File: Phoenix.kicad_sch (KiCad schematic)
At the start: 0 parts

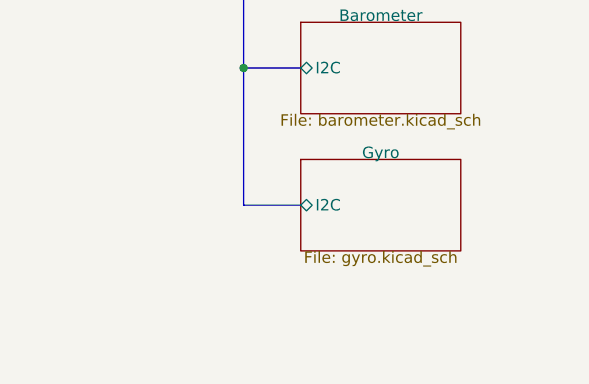
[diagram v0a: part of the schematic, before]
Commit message: Added pullup resistors
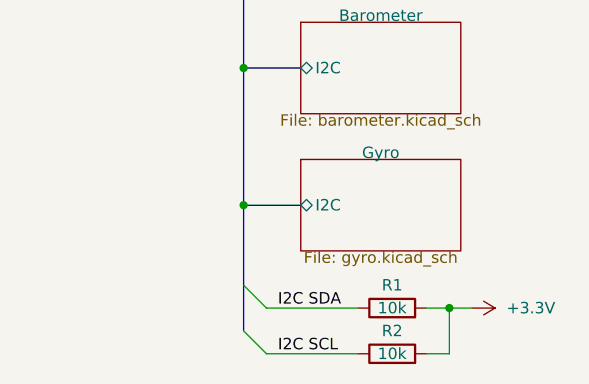
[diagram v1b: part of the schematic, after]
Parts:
- added R1, R2: 10k, symbol Device:R
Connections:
- new net +3V3: R1.2, R2.2
- new net I2C SCL: R2.1
- new net I2C SDA: R1.1
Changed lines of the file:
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@@
     (comment 1 "2022/10/18 WH")
   )
+  (junction (at 128.27 85.09) (diameter 0) (color 0 0 0 0)
+  )
   (junction (at 128.27 69.85) (diameter 0) (color 0 0 0 0)
   )
   (junction (at 128.27 54.61) (diameter 0) (color 0 0 0 0)
   )
+  (junction (at 151.13 96.52) (diameter 0) (color 0 0 0 0)
+  )
+  (bus_entry (at 130.81 96.52) (size -2.54 -2.54)
+    (stroke (width 0) (type default) (color 0 0 0 0))
+  )
+  (bus_entry (at 130.81 101.6) (size -2.54 -2.54)
+    (stroke (width 0) (type default) (color 0 0 0 0))
+  )
   (bus (pts (xy 128.27 46.99) (xy 128.27 36.83))
     (stroke (width 0) (type default) (color 0 0 0 0))
   )
+  (wire (pts (xy 151.13 101.6) (xy 148.59 101.6))
+    (stroke (width 0) (type default) (color 0 0 0 0))
+  )
+  (wire (pts (xy 148.59 96.52) (xy 151.13 96.52))
+    (stroke (width 0) (type default) (color 0 0 0 0))
+  )
   (bus (pts (xy 128.27 69.85) (xy 128.27 85.09))
     (stroke (width 0) (type default) (color 0 0 0 0))
@@
     (stroke (width 0) (type default) (color 0 0 0 0))
   )
+  (bus (pts (xy 128.27 93.98) (xy 128.27 99.06))
+    (stroke (width 0) (type default) (color 0 0 0 0))
+  )
+  (wire (pts (xy 151.13 96.52) (xy 153.67 96.52))
+    (stroke (width 0) (type default) (color 0 0 0 0))
+  )
+  (wire (pts (xy 130.81 101.6) (xy 140.97 101.6))
+    (stroke (width 0) (type default) (color 0 0 0 0))
+  )
   (bus (pts (xy 121.92 54.61) (xy 128.27 54.61))
     (stroke (width 0) (type default) (color 0 0 0 0))
@@
     (stroke (width 0) (type default) (color 0 0 0 0))
   )
+  (wire (pts (xy 130.81 96.52) (xy 140.97 96.52))
+    (stroke (width 0) (type default) (color 0 0 0 0))
+  )
   (bus (pts (xy 128.27 54.61) (xy 134.62 54.61))
     (stroke (width 0) (type default) (color 0 0 0 0))
   )
+  (bus (pts (xy 128.27 85.09) (xy 128.27 93.98))
+    (stroke (width 0) (type default) (color 0 0 0 0))
+  )
+  (wire (pts (xy 151.13 96.52) (xy 151.13 101.6))
+    (stroke (width 0) (type default) (color 0 0 0 0))
+  )
   (bus (pts (xy 128.27 85.09) (xy 134.62 85.09))
     (stroke (width 0) (type default) (color 0 0 0 0))
@@
   (bus (pts (xy 128.27 54.61) (xy 128.27 69.85))
     (stroke (width 0) (type default) (color 0 0 0 0))
+  )
+  (label "I2C SDA" (at 132.08 96.52 0)
+    (effects (font (size 1.27 1.27)) (justify left bottom))
+  )
+  (label "I2C SCL" (at 132.08 101.6 0)
+    (effects (font (size 1.27 1.27)) (justify left bottom))
+  )
+  (symbol (lib_id "Device:R") (at 144.78 101.6 90) (unit 1)
+    (in_bom yes) (on_board yes)
+    (property "Reference" "R2" (id 0) (at 144.78 99.06 90))
+    (property "Value" "10k" (id 1) (at 144.78 101.6 90))
+    (property "Footprint" "" (id 2) (at 144.78 103.378 90)
+      (effects (font (size 1.27 1.27)) hide)
+    )
+    (property "Datasheet" "~" (id 3) (at 144.78 101.6 0)
+      (effects (font (size 1.27 1.27)) hide)
+    )
+    (pin "1")
+    (pin "2")
+  )
+  (symbol (lib_id "Device:R") (at 144.78 96.52 90) (unit 1)
+    (in_bom yes) (on_board yes)
+    (property "Reference" "R1" (id 0) (at 144.78 93.98 90))
+    (property "Value" "10k" (id 1) (at 144.78 96.52 90))
+    (property "Footprint" "" (id 2) (at 144.78 98.298 90)
+      (effects (font (size 1.27 1.27)) hide)
+    )
+    (property "Datasheet" "~" (id 3) (at 144.78 96.52 0)
+      (effects (font (size 1.27 1.27)) hide)
+    )
+    (pin "1")
+    (pin "2")
+  )
+  (symbol (lib_id "power:+3.3V") (at 153.67 96.52 270) (unit 1)
+    (in_bom yes) (on_board yes) (fields_autoplaced)
+    (property "Reference" "#PWR?" (id 0) (at 149.86 96.52 0)
+      (effects (font (size 1.27 1.27)) hide)
+    )
+    (property "Value" "+3.3V" (id 1) (at 157.48 96.5199 90)
+      (effects (font (size 1.27 1.27)) (justify left))
+    )
+    (property "Footprint" "" (id 2) (at 153.67 96.52 0)
+      (effects (font (size 1.27 1.27)) hide)
+    )
+    (property "Datasheet" "" (id 3) (at 153.67 96.52 0)
+      (effects (font (size 1.27 1.27)) hide)
+    )
+    (pin "1")
   )
   (sheet (at 134.62 64.77) (size 17.78 10.16)
@@
       (reference "#PWR?") (unit 1) (value "GND") (footprint "")
     )
+    (path "/fdc5bc93-cd8d-4811-bebe-254f9b5ae1b6"
+      (reference "#PWR?") (unit 1) (value "+3.3V") (footprint "")
+    )
     (path "/973e92e2-e415-4dc5-9283-1d2d8aa34625/00b942de-1e62-476c-a78f-85d1dc0d5dee"
       (reference "C1") (unit 1) (value "100n") (footprint "Capacitor_SMD:C_0603_1608Metric")
@@
       (reference "R1") (unit 1) (value "27") (footprint "Resistor_SMD:R_0603_1608Metric_Pad0.98x0.95mm_HandSolder")
     )
+    (path "/db5533e2-fae3-4182-acad-2909cd70b23b"
+      (reference "R1") (unit 1) (value "10k") (footprint "")
+    )
     (path "/973e92e2-e415-4dc5-9283-1d2d8aa34625/365d1fd1-547e-42e3-ad75-f7c0cd8d8a12"
       (reference "R2") (unit 1) (value "27") (footprint "Resistor_SMD:R_0603_1608Metric_Pad0.98x0.95mm_HandSolder")
     )
+    (path "/c724a421-745b-4d41-9112-41d74b6d024a"
+      (reference "R2") (unit 1) (value "10k") (footprint "")
+    )
     (path "/973e92e2-e415-4dc5-9283-1d2d8aa34625/7239285e-3faf-4ba7-895f-832ed4958cbd"

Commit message: Experimented with git
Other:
- sheet Gyro renamed Accelerometer
- sheet Accelerometer: file gyro.kicad_sch -> accl.kicad_sch
- moved on the sheet: R1, R2

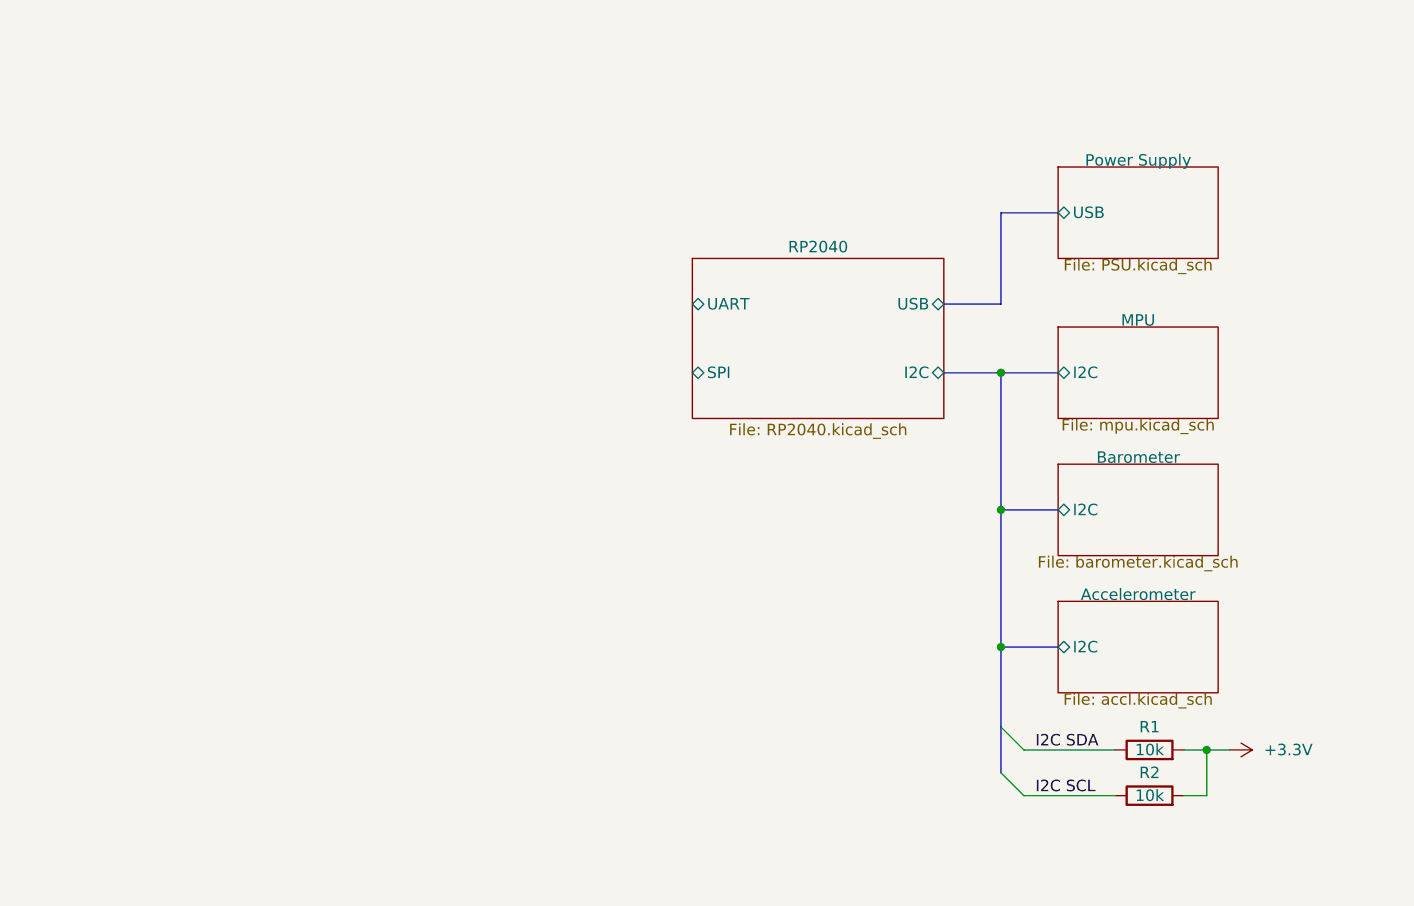
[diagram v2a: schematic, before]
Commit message: Added flash and radio submodules
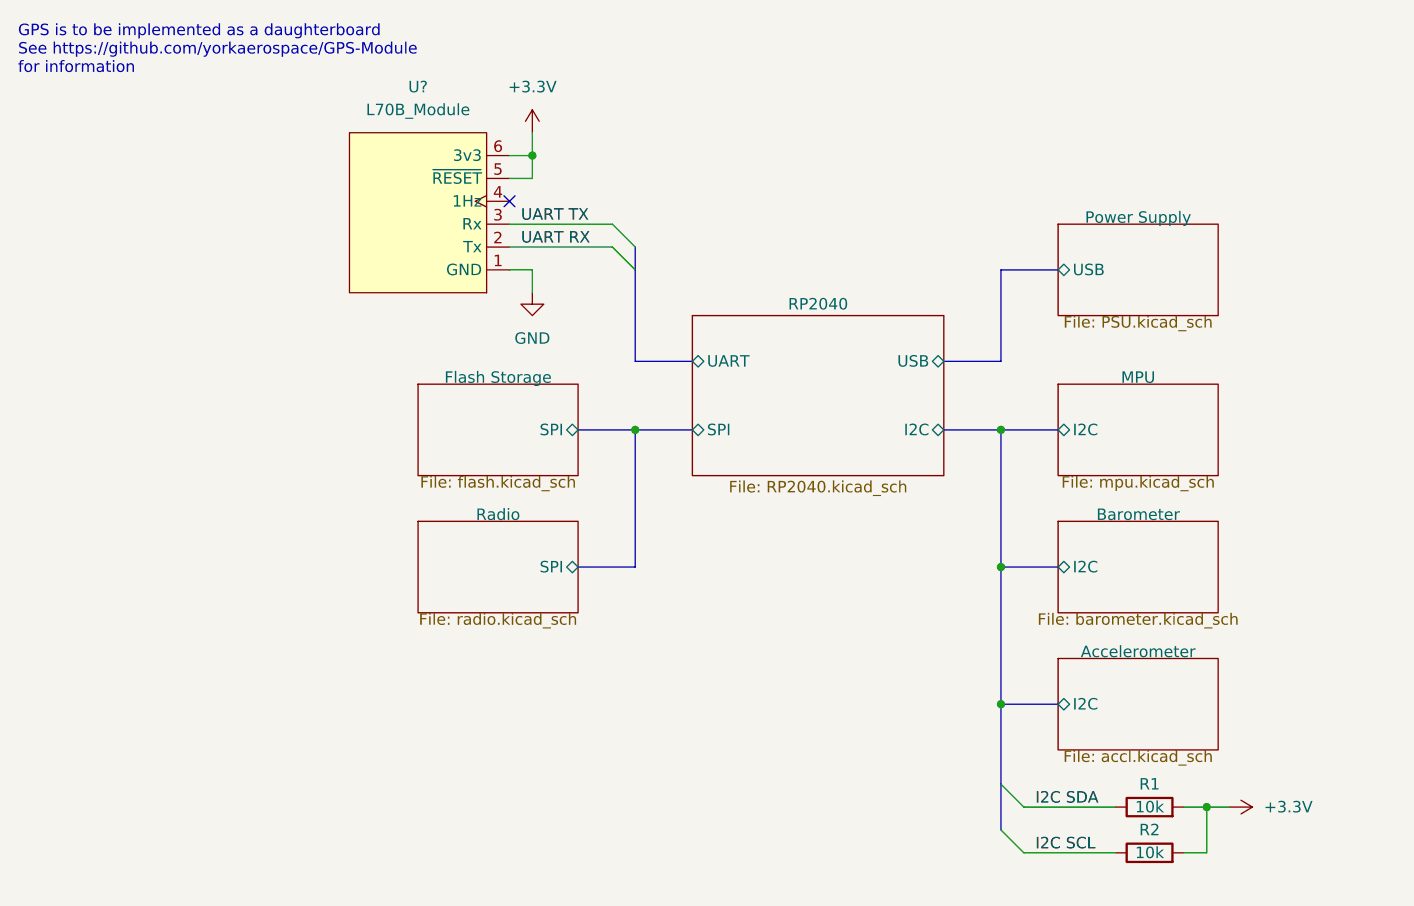
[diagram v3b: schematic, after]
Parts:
- added U?: L70B_Module, symbol GPS_Components:L70B_Module
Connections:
- net +3V3: now also U?.5 (~{RESET}), U?.6 (3v3)
- new net GND: U?.1 (GND)
- new net UART RX: U?.2 (Tx)
- new net UART TX: U?.3 (Rx)
- no-connect marks 0 -> 1
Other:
- added sheet Flash Storage (flash.kicad_sch)
- added sheet Radio (radio.kicad_sch)
- note added: "GPS is to be implemented as a daughterboard See https://github.com/yorkaerospace/GPS-Module for information"
- moved on the sheet: R1, R2

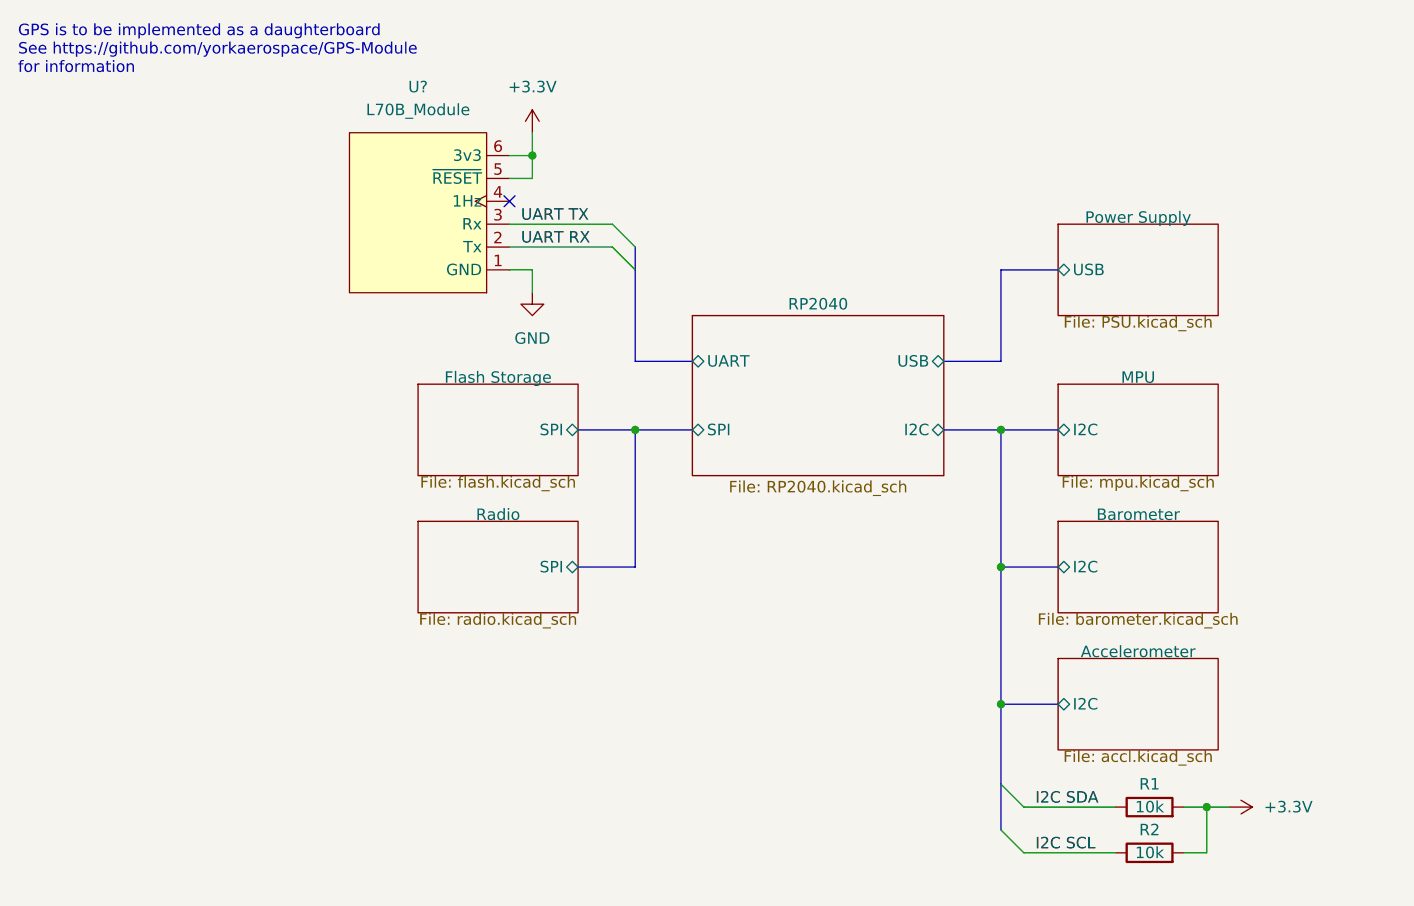
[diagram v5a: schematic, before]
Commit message: Fixed bus names
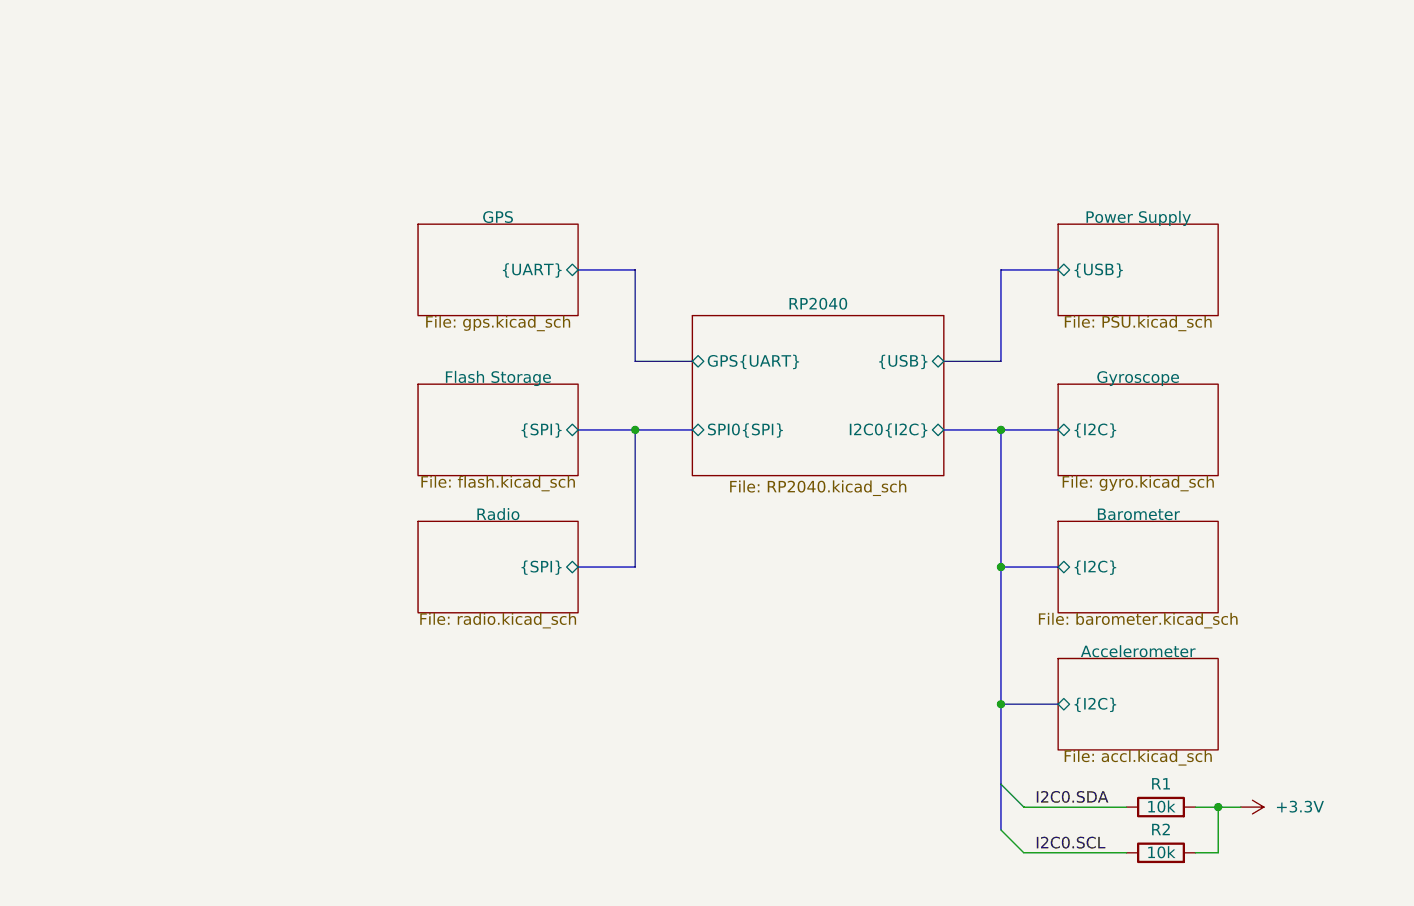
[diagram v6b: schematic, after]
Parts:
- removed U?: L70B_Module, symbol GPS_Components:L70B_Module
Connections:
- net I2C SCL renamed I2C0.SCL
- net I2C SDA renamed I2C0.SDA
- no-connect marks 1 -> 0
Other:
- sheet MPU renamed Gyroscope
- added sheet GPS (gps.kicad_sch)
- sheet Accelerometer ports: added {I2C}; removed I2C
- sheet Barometer ports: added {I2C}; removed I2C
- sheet Flash Storage ports: added {SPI}; removed SPI
- sheet Gyroscope: file mpu.kicad_sch -> gyro.kicad_sch
- sheet Gyroscope ports: added {I2C}; removed I2C
- sheet Power Supply ports: added {USB}; removed USB
- sheet RP2040 ports: added GPS{UART}, I2C0{I2C}, SPI0{SPI}, {USB}; removed I2C, SPI, UART, USB
- sheet Radio ports: added {SPI}; removed SPI
- note removed: "GPS is to be implemented as a daughterboard See https://github.com/yorkaerospace/GPS-Module for information"
- moved on the sheet: R1, R2

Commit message: Various updates because I forgot to commit for a while
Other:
- added sheet GPIO & Pyro (gpio.kicad_sch)
- sheet Accelerometer ports: added {INT}; removed none
- sheet Gyroscope ports: added {INT}; removed none
- sheet Power Supply ports: added VBat/4; removed none
- sheet RP2040 ports: added ADC, {GPIO}, {INT}; removed none
- sheet Radio ports: added {INT}; removed none
- moved on the sheet: R1, R2
